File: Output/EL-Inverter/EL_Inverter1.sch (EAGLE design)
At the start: 13 parts

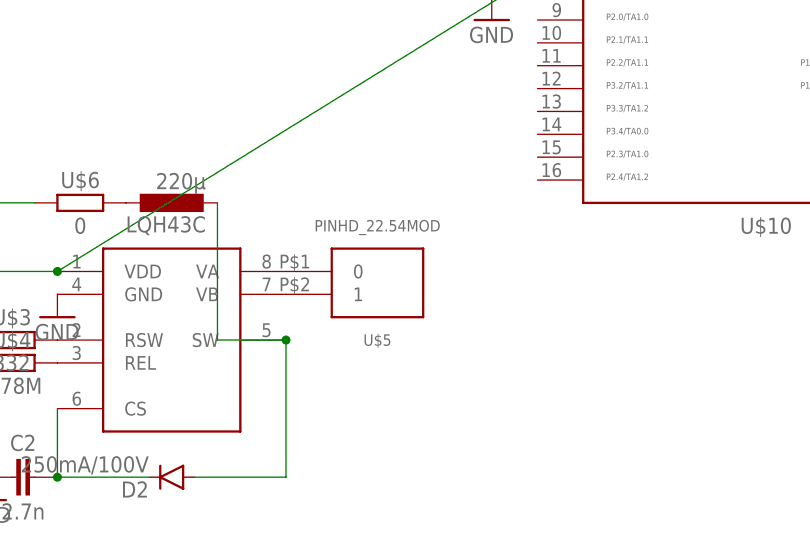
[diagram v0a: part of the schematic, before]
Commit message: Update Pinheader
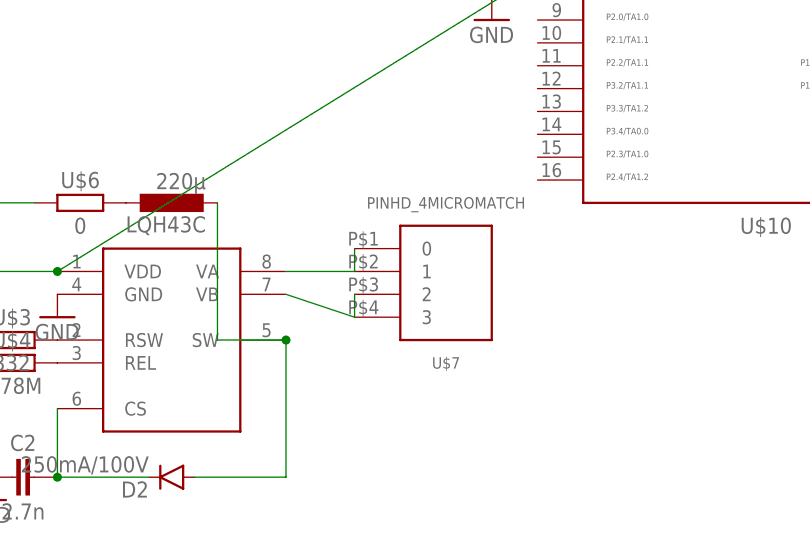
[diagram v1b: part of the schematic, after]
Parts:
- removed U$5: PINHD_22.54MOD, thar:PINHD_22.54MOD
- added U$7: PINHD_4MICROMATCH, thar:PINHD_4MICROMATCH
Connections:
- net N$14: now also U$7.0, U$7.1; no longer U$5.0
- net N$16: now also U$7.2, U$7.3; no longer U$5.1
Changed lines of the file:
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@@
 <grid distance="0.1" unitdist="inch" unit="inch" style="lines" multiple="1" display="no" altdistance="0.01" altunitdist="inch" altunit="inch"/>
 <layers>
-<layer number="1" name="Top" color="4" fill="1" visible="yes" active="no"/>
-<layer number="16" name="Bottom" color="1" fill="1" visible="yes" active="no"/>
-<layer number="17" name="Pads" color="2" fill="1" visible="yes" active="no"/>
-<layer number="18" name="Vias" color="2" fill="1" visible="yes" active="no"/>
-<layer number="19" name="Unrouted" color="6" fill="1" visible="yes" active="no"/>
-<layer number="20" name="Dimension" color="15" fill="1" visible="yes" active="no"/>
-<layer number="21" name="tPlace" color="7" fill="1" visible="yes" active="no"/>
-<layer number="22" name="bPlace" color="7" fill="1" visible="yes" active="no"/>
-<layer number="23" name="tOrigins" color="15" fill="1" visible="yes" active="no"/>
-<layer number="24" name="bOrigins" color="15" fill="1" visible="yes" active="no"/>
-<layer number="25" name="tNames" color="7" fill="1" visible="yes" active="no"/>
-<layer number="26" name="bNames" color="7" fill="1" visible="yes" active="no"/>
-<layer number="27" name="tValues" color="7" fill="1" visible="yes" active="no"/>
-<layer number="28" name="bValues" color="7" fill="1" visible="yes" active="no"/>
+<layer number="1" name="Top" color="4" fill="1" visible="no" active="no"/>
+<layer number="16" name="Bottom" color="1" fill="1" visible="no" active="no"/>
+<layer number="17" name="Pads" color="2" fill="1" visible="no" active="no"/>
+<layer number="18" name="Vias" color="2" fill="1" visible="no" active="no"/>
+<layer number="19" name="Unrouted" color="6" fill="1" visible="no" active="no"/>
+<layer number="20" name="Dimension" color="15" fill="1" visible="no" active="no"/>
+<layer number="21" name="tPlace" color="7" fill="1" visible="no" active="no"/>
+<layer number="22" name="bPlace" color="7" fill="1" visible="no" active="no"/>
+<layer number="23" name="tOrigins" color="15" fill="1" visible="no" active="no"/>
+<layer number="24" name="bOrigins" color="15" fill="1" visible="no" active="no"/>
+<layer number="25" name="tNames" color="7" fill="1" visible="no" active="no"/>
+<layer number="26" name="bNames" color="7" fill="1" visible="no" active="no"/>
+<layer number="27" name="tValues" color="7" fill="1" visible="no" active="no"/>
+<layer number="28" name="bValues" color="7" fill="1" visible="no" active="no"/>
 <layer number="29" name="tStop" color="7" fill="3" visible="no" active="no"/>
 <layer number="30" name="bStop" color="7" fill="6" visible="no" active="no"/>
@@
 <layer number="35" name="tGlue" color="7" fill="4" visible="no" active="no"/>
 <layer number="36" name="bGlue" color="7" fill="5" visible="no" active="no"/>
-<layer number="37" name="tTest" color="7" fill="1" visible="yes" active="no"/>
-<layer number="38" name="bTest" color="7" fill="1" visible="yes" active="no"/>
+<layer number="37" name="tTest" color="7" fill="1" visible="no" active="no"/>
+<layer number="38" name="bTest" color="7" fill="1" visible="no" active="no"/>
 <layer number="39" name="tKeepout" color="4" fill="11" visible="no" active="no"/>
 <layer number="40" name="bKeepout" color="1" fill="11" visible="no" active="no"/>
@@
 <layer number="44" name="Drills" color="7" fill="1" visible="no" active="no"/>
 <layer number="45" name="Holes" color="7" fill="1" visible="no" active="no"/>
-<layer number="46" name="Milling" color="3" fill="1" visible="yes" active="no"/>
-<layer number="47" name="Measures" color="7" fill="1" visible="yes" active="no"/>
-<layer number="48" name="Document" color="7" fill="1" visible="yes" active="no"/>
-<layer number="49" name="Reference" color="7" fill="1" visible="yes" active="no"/>
-<layer number="50" name="dxf" color="7" fill="1" visible="yes" active="no"/>
-<layer number="51" name="tDocu" color="7" fill="1" visible="yes" active="no"/>
-<layer number="52" name="bDocu" color="7" fill="1" visible="yes" active="no"/>
-<layer number="53" name="tGND_GNDA" color="7" fill="9" visible="yes" active="no"/>
-<layer number="54" name="bGND_GNDA" color="1" fill="9" visible="yes" active="no"/>
-<layer number="56" name="wert" color="7" fill="1" visible="yes" active="no"/>
-<layer number="57" name="tCAD" color="7" fill="1" visible="yes" active="no"/>
+<layer number="46" name="Milling" color="3" fill="1" visible="no" active="no"/>
+<layer number="47" name="Measures" color="7" fill="1" visible="no" active="no"/>
+<layer number="48" name="Document" color="7" fill="1" visible="no" active="no"/>
+<layer number="49" name="Reference" color="7" fill="1" visible="no" active="no"/>
+<layer number="50" name="dxf" color="7" fill="1" visible="no" active="no"/>
+<layer number="51" name="tDocu" color="7" fill="1" visible="no" active="no"/>
+<layer number="52" name="bDocu" color="7" fill="1" visible="no" active="no"/>
+<layer number="53" name="tGND_GNDA" color="7" fill="9" visible="no" active="no"/>
+<layer number="54" name="bGND_GNDA" color="1" fill="9" visible="no" active="no"/>
+<layer number="56" name="wert" color="7" fill="1" visible="no" active="no"/>
+<layer number="57" name="tCAD" color="7" fill="1" visible="no" active="no"/>
 <layer number="90" name="Modules" color="5" fill="1" visible="yes" active="yes"/>
 <layer number="91" name="Nets" color="2" fill="1" visible="yes" active="yes"/>
@@
 <part name="P+1" library="supply1" deviceset="VCC" device=""/>
 <part name="GND8" library="supply1" deviceset="GND" device=""/>
-<part name="U$5" library="thar" deviceset="PINHD_2" device="2.54MOD"/>
 <part name="U$6" library="thar" deviceset="RESISTOR" device="0603" value="0"/>
+<part name="U$7" library="thar" deviceset="PINHD_4" device="MICROMATCH"/>
 </parts>
 <sheets>
@@
 <instance part="P+1" gate="VCC" x="152.4" y="106.68"/>
 <instance part="GND8" gate="1" x="144.78" y="104.14"/>
-<instance part="U$5" gate="G$1" x="58.42" y="66.04"/>
 <instance part="U$6" gate="G$1" x="25.4" y="76.2"/>
+<instance part="U$7" gate="G$1" x="66.04" y="68.58"/>
 </instances>
 <busses>
@@
 </segment>
 </net>
-<net name="N$14" class="0">
-<segment>
-<pinref part="U$8" gate="A" pin="VA"/>
-<pinref part="U$5" gate="G$1" pin="0"/>
-</segment>
-</net>
-<net name="N$16" class="0">
-<segment>
-<pinref part="U$8" gate="A" pin="VB"/>
-<pinref part="U$5" gate="G$1" pin="1"/>
-</segment>
-</net>
 <net name="N$2" class="0">
 <segment>
@@
 </segment>
 </net>
+<net name="N$14" class="0">
+<segment>
+<pinref part="U$8" gate="A" pin="VA"/>
+<pinref part="U$7" gate="G$1" pin="1"/>
+<wire x1="55.88" y1="68.58" x2="48.26" y2="68.58" width="0.1524" layer="91"/>
+<pinref part="U$7" gate="G$1" pin="0"/>
+<wire x1="55.88" y1="68.58" x2="55.88" y2="71.12" width="0.1524" layer="91"/>
+</segment>
+</net>
+<net name="N$16" class="0">
+<segment>
+<pinref part="U$8" gate="A" pin="VB"/>
+<pinref part="U$7" gate="G$1" pin="3"/>
+<wire x1="48.26" y1="66.04" x2="55.88" y2="63.5" width="0.1524" layer="91"/>
+<pinref part="U$7" gate="G$1" pin="2"/>
+<wire x1="55.88" y1="66.04" x2="55.88" y2="63.5" width="0.1524" layer="91"/>
+</segment>
+</net>
